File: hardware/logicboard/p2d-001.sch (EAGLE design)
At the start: 68 parts, among them IC1 74LS06N, IC2 4066N, IC3 MAX3468CPA, J1 MKR, J10 THS, J2 GPIO, J3 Vcc, J4 RLY, J5 SPI, J6 LED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

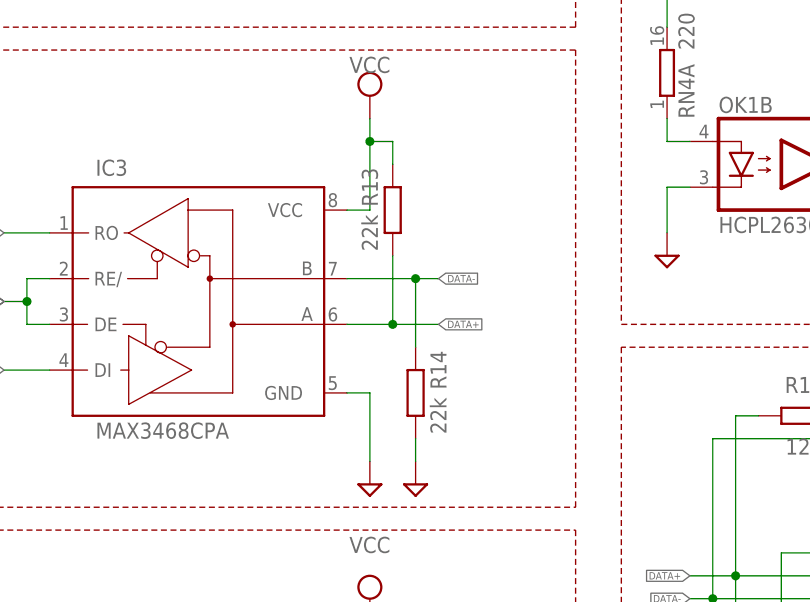
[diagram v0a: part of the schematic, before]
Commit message: Changed DMX pull-up/down resisters to surface mount.
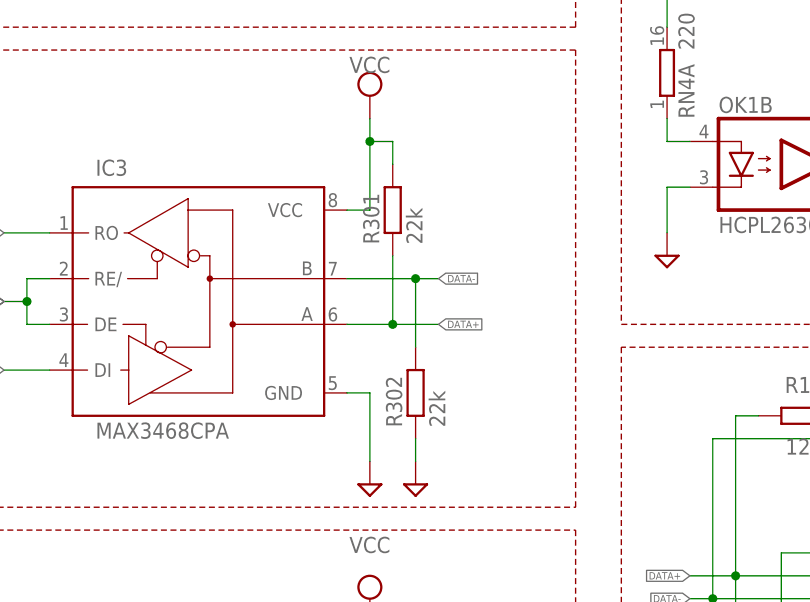
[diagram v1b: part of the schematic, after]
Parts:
- removed R13, R14: 22k, resistor:R-EU_0204/5
- added R301, R302: 22k, rcl:R-EU_M2012
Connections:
- net DATA+: now also R301.1; no longer R13.1
- net DATA-: now also R302.2; no longer R14.2
- net GND: now also R302.1; no longer R14.1
- net VCC: now also R301.2; no longer R13.2
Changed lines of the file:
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@@
 <part name="C11" library="resistor" library_urn="urn:adsk.eagle:library:348" deviceset="C-EU" device="025-024X044" package3d_urn="urn:adsk.eagle:package:23630/1" value="100n"/>
 <part name="SUPPLY8" library="supply2" deviceset="GND" device=""/>
-<part name="R13" library="resistor" library_urn="urn:adsk.eagle:library:348" deviceset="R-EU_" device="0204/5" package3d_urn="urn:adsk.eagle:package:23488/1" value="22k"/>
-<part name="R14" library="resistor" library_urn="urn:adsk.eagle:library:348" deviceset="R-EU_" device="0204/5" package3d_urn="urn:adsk.eagle:package:23488/1" value="22k"/>
 <part name="SUPPLY9" library="supply2" library_urn="urn:adsk.eagle:library:372" deviceset="VCC" device=""/>
 <part name="SUPPLY15" library="supply2" library_urn="urn:adsk.eagle:library:372" deviceset="VCC" device=""/>
@@
 <part name="SUPPLY21" library="supply2" library_urn="urn:adsk.eagle:library:372" deviceset="VCC" device=""/>
 <part name="SUPPLY22" library="supply2" deviceset="GND" device=""/>
+<part name="R301" library="rcl" library_urn="urn:adsk.eagle:library:334" deviceset="R-EU_" device="M2012" package3d_urn="urn:adsk.eagle:package:23561/2" value="22k"/>
+<part name="R302" library="rcl" library_urn="urn:adsk.eagle:library:334" deviceset="R-EU_" device="M2012" package3d_urn="urn:adsk.eagle:package:23561/2" value="22k"/>
 </parts>
 <sheets>
@@
 </instance>
 <instance part="SUPPLY8" gate="GND" x="299.72" y="198.12" smashed="yes"/>
-<instance part="R13" gate="G$1" x="182.88" y="81.28" smashed="yes" rot="R90">
-<attribute name="NAME" x="180.34" y="83.82" size="1.778" layer="95" rot="R90" align="center"/>
-<attribute name="VALUE" x="180.34" y="78.74" size="1.778" layer="96" rot="R90" align="center"/>
-</instance>
-<instance part="R14" gate="G$1" x="185.42" y="60.96" smashed="yes" rot="R90">
-<attribute name="NAME" x="187.96" y="63.5" size="1.778" layer="95" rot="R90" align="center"/>
-<attribute name="VALUE" x="187.96" y="58.42" size="1.778" layer="96" rot="R90" align="center"/>
-</instance>
 <instance part="SUPPLY9" gate="G$1" x="53.34" y="246.38" smashed="yes">
 <attribute name="VALUE" x="53.34" y="251.46" size="1.778" layer="96" align="bottom-center"/>
@@
 </instance>
 <instance part="SUPPLY22" gate="GND" x="185.42" y="50.8" smashed="yes"/>
+<instance part="R301" gate="G$1" x="182.88" y="81.28" smashed="yes" rot="R90">
+<attribute name="NAME" x="181.3814" y="77.47" size="1.778" layer="95" rot="R90"/>
+<attribute name="VALUE" x="186.182" y="77.47" size="1.778" layer="96" rot="R90"/>
+</instance>
+<instance part="R302" gate="G$1" x="185.42" y="60.96" smashed="yes" rot="R90">
+<attribute name="NAME" x="183.9214" y="57.15" size="1.778" layer="95" rot="R90"/>
+<attribute name="VALUE" x="188.722" y="57.15" size="1.778" layer="96" rot="R90"/>
+</instance>
 </instances>
 <busses>
@@
 </segment>
 <segment>
-<pinref part="R14" gate="G$1" pin="1"/>
 <wire x1="185.42" y1="55.88" x2="185.42" y2="53.34" width="0.1524" layer="91"/>
 <pinref part="SUPPLY22" gate="GND" pin="GND"/>
+<pinref part="R302" gate="G$1" pin="1"/>
 </segment>
 </net>
@@
 <wire x1="177.8" y1="81.28" x2="180.34" y2="81.28" width="0.1524" layer="91"/>
 <wire x1="180.34" y1="81.28" x2="180.34" y2="88.9" width="0.1524" layer="91"/>
-<pinref part="R13" gate="G$1" pin="2"/>
 <wire x1="182.88" y1="86.36" x2="182.88" y2="88.9" width="0.1524" layer="91"/>
 <wire x1="182.88" y1="88.9" x2="180.34" y2="88.9" width="0.1524" layer="91"/>
@@
 <pinref part="SUPPLY18" gate="G$1" pin="VCC"/>
 <wire x1="180.34" y1="88.9" x2="180.34" y2="91.44" width="0.1524" layer="91"/>
+<pinref part="R301" gate="G$1" pin="2"/>
 </segment>
 <segment>
@@
 <label x="187.96" y="68.58" size="0.8128" layer="95" xref="yes"/>
 <wire x1="177.8" y1="68.58" x2="182.88" y2="68.58" width="0.1524" layer="91"/>
-<pinref part="R13" gate="G$1" pin="1"/>
 <wire x1="182.88" y1="68.58" x2="187.96" y2="68.58" width="0.1524" layer="91"/>
 <wire x1="182.88" y1="76.2" x2="182.88" y2="68.58" width="0.1524" layer="91"/>
 <junction x="182.88" y="68.58"/>
+<pinref part="R301" gate="G$1" pin="1"/>
 </segment>
 </net>
@@
 <wire x1="177.8" y1="73.66" x2="185.42" y2="73.66" width="0.1524" layer="91"/>
 <label x="187.96" y="73.66" size="0.8128" layer="95" xref="yes"/>
-<pinref part="R14" gate="G$1" pin="2"/>
 <wire x1="185.42" y1="73.66" x2="187.96" y2="73.66" width="0.1524" layer="91"/>
 <wire x1="185.42" y1="73.66" x2="185.42" y2="66.04" width="0.1524" layer="91"/>
 <junction x="185.42" y="73.66"/>
-</segment>
-</net>
+<pinref part="R302" gate="G$1" pin="2"/>
+</segment>
+</net>

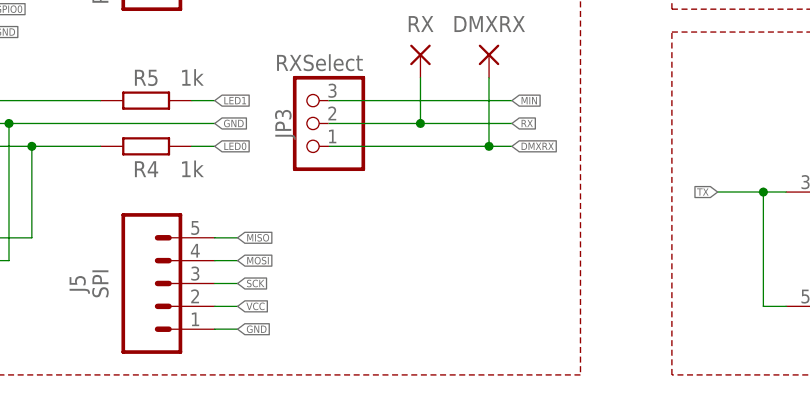
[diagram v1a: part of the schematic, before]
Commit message: Added restricted zone, added J11 for panel-mount XLR con.
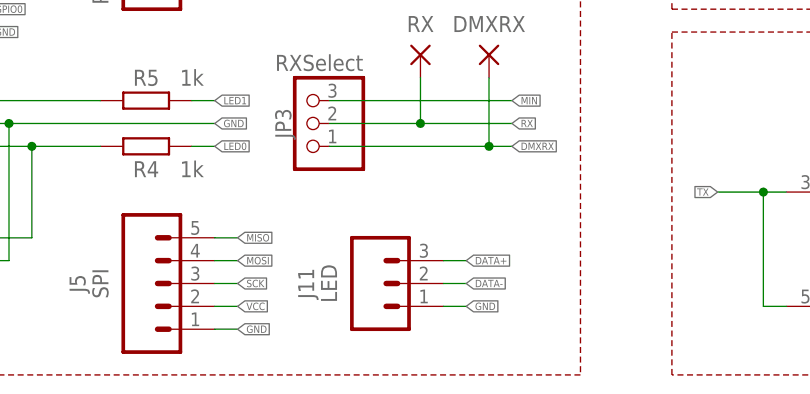
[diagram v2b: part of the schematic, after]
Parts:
- added J11: LED, SparkFun-Connectors:CONN_03JST-PTH-VERT
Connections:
- net DATA+: now also J11.3
- net DATA-: now also J11.2
- net GND: now also J11.1
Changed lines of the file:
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@@
 <part name="R301" library="rcl" library_urn="urn:adsk.eagle:library:334" deviceset="R-EU_" device="M2012" package3d_urn="urn:adsk.eagle:package:23561/2" value="22k"/>
 <part name="R302" library="rcl" library_urn="urn:adsk.eagle:library:334" deviceset="R-EU_" device="M2012" package3d_urn="urn:adsk.eagle:package:23561/2" value="22k"/>
+<part name="J11" library="SparkFun-Connectors" library_urn="urn:adsk.eagle:library:513" deviceset="CONN_03" device="JST-PTH-VERT" package3d_urn="urn:adsk.eagle:package:38080/1" value="LED"/>
 </parts>
 <sheets>
@@
 <attribute name="VALUE" x="188.722" y="57.15" size="1.778" layer="96" rot="R90"/>
 </instance>
+<instance part="J11" gate="J$1" x="88.9" y="17.78" smashed="yes">
+<attribute name="VALUE" x="83.82" y="17.78" size="1.778" layer="96" rot="R90" align="center"/>
+<attribute name="NAME" x="81.28" y="17.78" size="1.778" layer="95" rot="R90" align="center"/>
+</instance>
 </instances>
 <busses>
@@
 <pinref part="R302" gate="G$1" pin="1"/>
 </segment>
+<segment>
+<pinref part="J11" gate="J$1" pin="1"/>
+<wire x1="96.52" y1="15.24" x2="99.06" y2="15.24" width="0.1524" layer="91"/>
+<label x="99.06" y="15.24" size="0.8128" layer="95" xref="yes"/>
+</segment>
 </net>
 <net name="VCC" class="2">
@@
 <pinref part="R301" gate="G$1" pin="1"/>
 </segment>
+<segment>
+<pinref part="J11" gate="J$1" pin="3"/>
+<wire x1="96.52" y1="20.32" x2="99.06" y2="20.32" width="0.1524" layer="91"/>
+<label x="99.06" y="20.32" size="0.8128" layer="95" xref="yes"/>
+</segment>
 </net>
 <net name="DATA-" class="0">
@@
 <pinref part="R302" gate="G$1" pin="2"/>
 </segment>
-</net>
+<segment>
+<pinref part="J11" gate="J$1" pin="2"/>
+<wire x1="96.52" y1="17.78" x2="99.06" y2="17.78" width="0.1524" layer="91"/>
+<label x="99.06" y="17.78" size="0.8128" layer="95" xref="yes"/>
+</segment>
+</net>

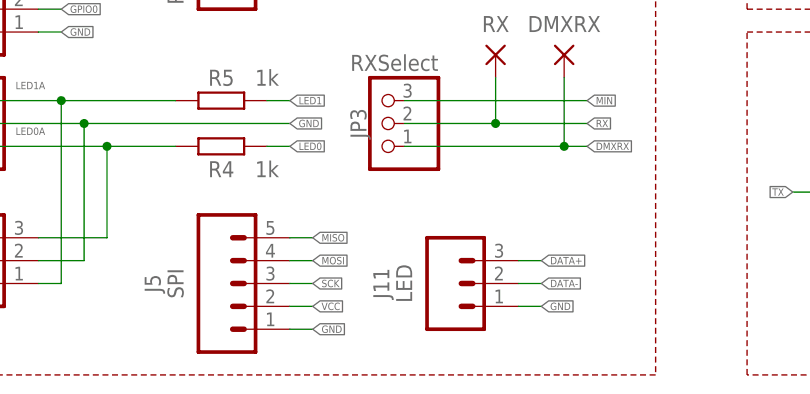
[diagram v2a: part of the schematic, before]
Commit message: Renamed J11 to XLR.
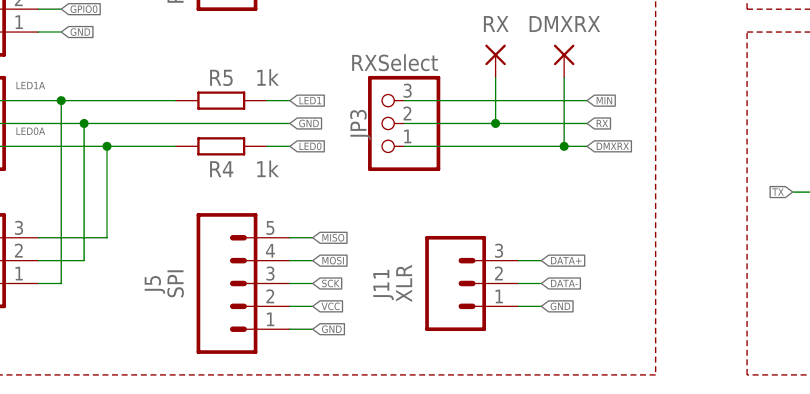
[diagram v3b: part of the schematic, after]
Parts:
- J11: value LED -> XLR
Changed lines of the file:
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@@
 <part name="R301" library="rcl" library_urn="urn:adsk.eagle:library:334" deviceset="R-EU_" device="M2012" package3d_urn="urn:adsk.eagle:package:23561/2" value="22k"/>
 <part name="R302" library="rcl" library_urn="urn:adsk.eagle:library:334" deviceset="R-EU_" device="M2012" package3d_urn="urn:adsk.eagle:package:23561/2" value="22k"/>
-<part name="J11" library="SparkFun-Connectors" library_urn="urn:adsk.eagle:library:513" deviceset="CONN_03" device="JST-PTH-VERT" package3d_urn="urn:adsk.eagle:package:38080/1" value="LED"/>
+<part name="J11" library="SparkFun-Connectors" library_urn="urn:adsk.eagle:library:513" deviceset="CONN_03" device="JST-PTH-VERT" package3d_urn="urn:adsk.eagle:package:38080/1" value="XLR"/>
 </parts>
 <sheets>

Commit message: Changed silk of JP10.
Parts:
- JP10: device pinhead:PINHD-1X2/90 -> pinhead:PINHD-1X2
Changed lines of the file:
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@@
 <part name="R10" library="resistor" library_urn="urn:adsk.eagle:library:348" deviceset="R-EU_" device="0204/5" package3d_urn="urn:adsk.eagle:package:23488/1" value="120"/>
 <part name="SUPPLY10" library="supply2" deviceset="GND" device=""/>
-<part name="JP10" library="pinhead" library_urn="urn:adsk.eagle:library:325" deviceset="PINHD-1X2" device="/90" package3d_urn="urn:adsk.eagle:package:22437/2" value="SelfTerminate"/>
+<part name="JP10" library="pinhead" library_urn="urn:adsk.eagle:library:325" deviceset="PINHD-1X2" device="" package3d_urn="urn:adsk.eagle:package:22435/2" value="SelfTerminate"/>
 <part name="SUPPLY14" library="supply2" deviceset="GND" device=""/>
 <part name="IC1" library="74xx-us" library_urn="urn:adsk.eagle:library:88" deviceset="74*06" device="N" package3d_urn="urn:adsk.eagle:package:16407/2" technology="LS"/>

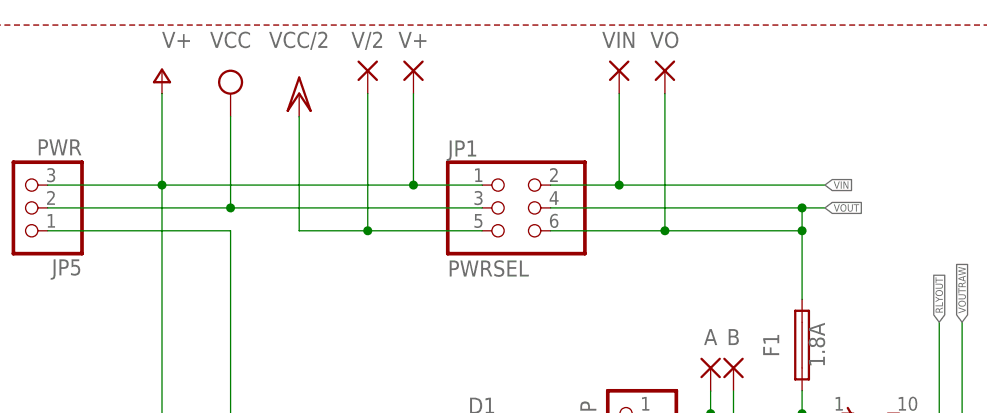
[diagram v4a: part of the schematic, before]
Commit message: Removed power pads.
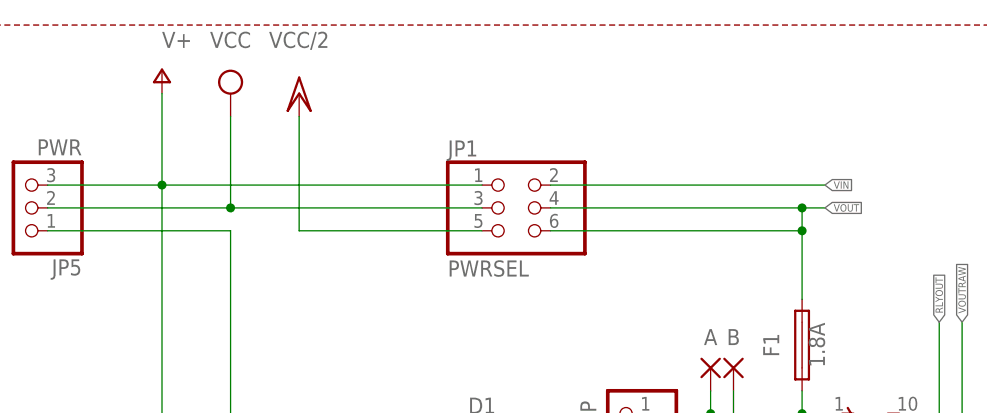
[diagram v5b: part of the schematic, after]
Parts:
- removed V+, V/2, VIN, VO: (no value), wirepad:SMD2
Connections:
- net V+: no longer V+.P
- net VCC/2: no longer V/2.P
- net VIN: no longer VIN.P
- net VOUT: no longer VO.P
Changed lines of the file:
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@@
 <part name="OK1" library="optocoupler" library_urn="urn:adsk.eagle:library:320" deviceset="HCPL2630" device="" package3d_urn="urn:adsk.eagle:package:21941/1"/>
 <part name="SUPPLY1" library="supply2" deviceset="GND" device=""/>
-<part name="V+" library="wirepad" library_urn="urn:adsk.eagle:library:412" deviceset="SMD2" device="" package3d_urn="urn:adsk.eagle:package:30839/1"/>
-<part name="VIN" library="wirepad" library_urn="urn:adsk.eagle:library:412" deviceset="SMD2" device="" package3d_urn="urn:adsk.eagle:package:30839/1"/>
 <part name="J0" library="con-jack" library_urn="urn:adsk.eagle:library:154" deviceset="JACK-PLUG" device="0" package3d_urn="urn:adsk.eagle:package:7492/1"/>
 <part name="R4" library="resistor" library_urn="urn:adsk.eagle:library:348" deviceset="R-EU_" device="0204/5" package3d_urn="urn:adsk.eagle:package:23488/1" value="1k"/>
@@
 <part name="SV2" library="pinhead" library_urn="urn:adsk.eagle:library:325" deviceset="PINHD-2X10" device="" package3d_urn="urn:adsk.eagle:package:22405/2" value="Backport II"/>
 <part name="SV3" library="pinhead" library_urn="urn:adsk.eagle:library:325" deviceset="PINHD-2X7" device="" package3d_urn="urn:adsk.eagle:package:22478/2" value="Testport II"/>
-<part name="V/2" library="wirepad" library_urn="urn:adsk.eagle:library:412" deviceset="SMD2" device="" package3d_urn="urn:adsk.eagle:package:30839/1"/>
-<part name="VO" library="wirepad" library_urn="urn:adsk.eagle:library:412" deviceset="SMD2" device="" package3d_urn="urn:adsk.eagle:package:30839/1"/>
 <part name="A" library="wirepad" library_urn="urn:adsk.eagle:library:412" deviceset="SMD2" device="" package3d_urn="urn:adsk.eagle:package:30839/1"/>
 <part name="B" library="wirepad" library_urn="urn:adsk.eagle:library:412" deviceset="SMD2" device="" package3d_urn="urn:adsk.eagle:package:30839/1"/>
@@
 </instance>
 <instance part="SUPPLY1" gate="GND" x="213.36" y="76.2" smashed="yes"/>
-<instance part="V+" gate="1" x="73.66" y="248.92" smashed="yes" rot="R270">
-<attribute name="NAME" x="73.66" y="251.46" size="1.778" layer="95" align="bottom-center"/>
-<attribute name="VALUE" x="70.358" y="250.063" size="1.778" layer="96" rot="R270"/>
-</instance>
-<instance part="VIN" gate="1" x="96.52" y="248.92" smashed="yes" rot="R270">
-<attribute name="NAME" x="96.52" y="251.46" size="1.778" layer="95" align="bottom-center"/>
-<attribute name="VALUE" x="93.218" y="250.063" size="1.778" layer="96" rot="R270"/>
-</instance>
 <instance part="J0" gate="G$1" x="33.02" y="198.12" smashed="yes">
 <attribute name="NAME" x="25.4" y="203.2" size="1.778" layer="95"/>
@@
 <attribute name="NAME" x="328.93" y="59.055" size="1.778" layer="95"/>
 <attribute name="VALUE" x="328.93" y="35.56" size="1.778" layer="96"/>
-</instance>
-<instance part="V/2" gate="1" x="68.58" y="248.92" smashed="yes" rot="R270">
-<attribute name="NAME" x="68.58" y="251.46" size="1.778" layer="95" align="bottom-center"/>
-<attribute name="VALUE" x="65.278" y="250.063" size="1.778" layer="96" rot="R270"/>
-</instance>
-<instance part="VO" gate="1" x="101.6" y="248.92" smashed="yes" rot="R270">
-<attribute name="NAME" x="101.6" y="251.46" size="1.778" layer="95" align="bottom-center"/>
-<attribute name="VALUE" x="98.298" y="250.063" size="1.778" layer="96" rot="R270"/>
 </instance>
 <instance part="A" gate="1" x="106.68" y="215.9" smashed="yes" rot="R270">
@@
 <segment>
 <pinref part="JP1" gate="A" pin="2"/>
-<wire x1="88.9" y1="236.22" x2="96.52" y2="236.22" width="0.1524" layer="91"/>
 <label x="119.38" y="236.22" size="0.8128" layer="95" xref="yes"/>
-<wire x1="96.52" y1="236.22" x2="119.38" y2="236.22" width="0.1524" layer="91"/>
-<wire x1="96.52" y1="236.22" x2="96.52" y2="246.38" width="0.1524" layer="91"/>
-<junction x="96.52" y="236.22"/>
-<pinref part="VIN" gate="1" pin="P"/>
+<wire x1="88.9" y1="236.22" x2="119.38" y2="236.22" width="0.1524" layer="91"/>
 </segment>
 </net>
@@
 <wire x1="60.96" y1="243.84" x2="60.96" y2="231.14" width="0.1524" layer="91"/>
 <pinref part="JP1" gate="A" pin="5"/>
-<wire x1="81.28" y1="231.14" x2="68.58" y2="231.14" width="0.1524" layer="91"/>
-<pinref part="V/2" gate="1" pin="P"/>
-<wire x1="68.58" y1="231.14" x2="60.96" y2="231.14" width="0.1524" layer="91"/>
-<wire x1="68.58" y1="246.38" x2="68.58" y2="231.14" width="0.1524" layer="91"/>
-<junction x="68.58" y="231.14"/>
+<wire x1="81.28" y1="231.14" x2="60.96" y2="231.14" width="0.1524" layer="91"/>
 </segment>
 <segment>
@@
 <segment>
 <pinref part="JP1" gate="A" pin="6"/>
-<wire x1="88.9" y1="231.14" x2="101.6" y2="231.14" width="0.1524" layer="91"/>
 <pinref part="F1" gate="1" pin="2"/>
 <pinref part="JP1" gate="A" pin="4"/>
-<wire x1="101.6" y1="231.14" x2="116.84" y2="231.14" width="0.1524" layer="91"/>
+<wire x1="88.9" y1="231.14" x2="116.84" y2="231.14" width="0.1524" layer="91"/>
 <wire x1="88.9" y1="233.68" x2="116.84" y2="233.68" width="0.1524" layer="91"/>
 <label x="119.38" y="233.68" size="0.8128" layer="95" xref="yes"/>
@@
 <wire x1="116.84" y1="231.14" x2="116.84" y2="233.68" width="0.1524" layer="91"/>
 <junction x="116.84" y="231.14"/>
-<pinref part="VO" gate="1" pin="P"/>
-<wire x1="101.6" y1="246.38" x2="101.6" y2="231.14" width="0.1524" layer="91"/>
-<junction x="101.6" y="231.14"/>
 </segment>
 </net>
@@
 <pinref part="JP1" gate="A" pin="1"/>
 <wire x1="45.72" y1="200.66" x2="63.5" y2="200.66" width="0.1524" layer="91"/>
-<wire x1="81.28" y1="236.22" x2="73.66" y2="236.22" width="0.1524" layer="91"/>
-<wire x1="73.66" y1="236.22" x2="45.72" y2="236.22" width="0.1524" layer="91"/>
-<wire x1="73.66" y1="236.22" x2="73.66" y2="246.38" width="0.1524" layer="91"/>
-<junction x="73.66" y="236.22"/>
-<pinref part="V+" gate="1" pin="P"/>
+<wire x1="81.28" y1="236.22" x2="45.72" y2="236.22" width="0.1524" layer="91"/>
 <pinref part="P+3" gate="1" pin="V+"/>
 <wire x1="45.72" y1="246.38" x2="45.72" y2="236.22" width="0.1524" layer="91"/>
